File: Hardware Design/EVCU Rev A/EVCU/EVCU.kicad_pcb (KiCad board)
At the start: 4 copper layers, 121.9 x 86.4 mm, 91 parts, among them J1 Conn_01x06, J2 Conn_01x02, J3 APPS/BSE_Conn, J4 Micro_SD_Card, J5 DB9_Male, J6 Conn_01x02, Q1 Q_PMOS_GSD, U1 AZ1117-3.3, U10 EMIF06-MSD02N16, U11 ESDALC6V1W5, U2 AP62250WU-7, U3 STM32L4R9ZITx, U4 LM358, U5 MPU-6500, U6 SN65HVD230, U7 LM358, U9 ESDCAN24-2BLY, X1 ECS-2520MV-160-CN-TR

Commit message: bom. pcb. exports
- updated bom added q1, some other capacitors. updated component costs
- added logo to pcb
- changed swd pins to female socket
- exported gerbers
- filled out digikey order form
- filled out amazon order form
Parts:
- added G***: LOGO, LOGO, F.Cu at (108.0, 88.9)
- J1: footprint Connector_PinHeader_2.54mm:PinHeader_1x06_P2.54mm_Vertical -> Connector_PinSocket_2.54mm:PinSocket_1x06_P2.54mm_Vertical
- moved J3 0.86 mm to (18.8, 90.2)
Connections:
- net Net-(F1-Pad) renamed /F_OUT
- net Net-(J2-Pad1) renamed /F_IN
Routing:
- net /VPA_BSE: track 11.5 -> 12.4 mm
- net /VPA_2: track 10.7 -> 11.6 mm
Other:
- board text added: "VPA2"
- board text removed: "VPA 2"

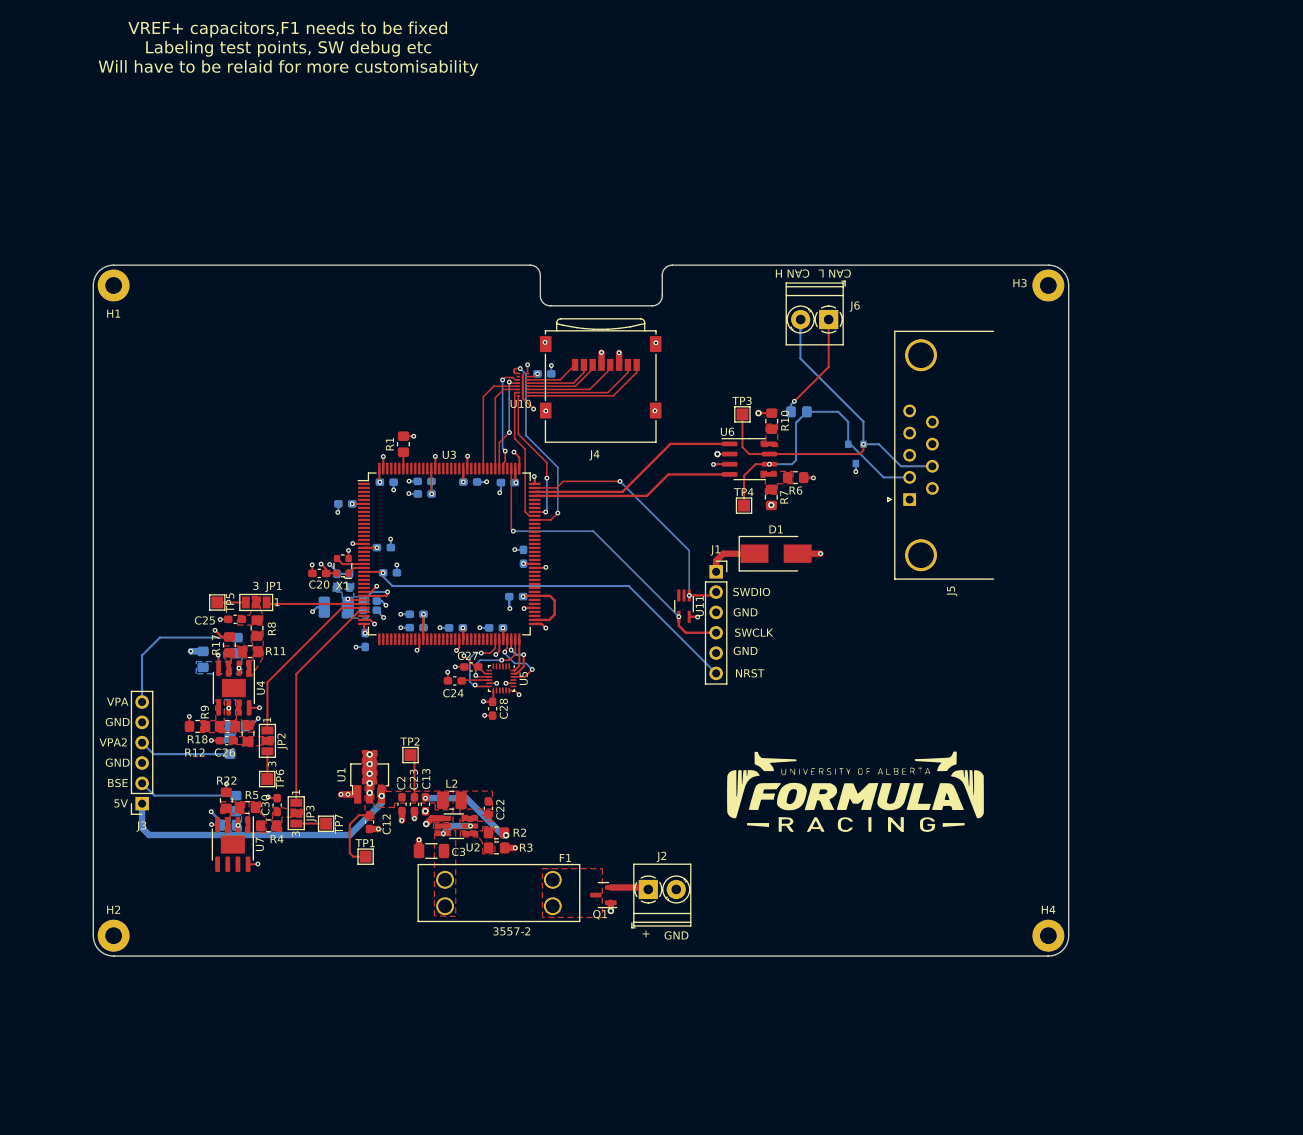
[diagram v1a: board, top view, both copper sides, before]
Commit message: pcb and bom
- moved mcu capacitors to top layer
- rearranged components to shrink pcb
- replaced j3 with 1x06 phoenix connector
- replaced j6 with 1x02 male 2.54 header
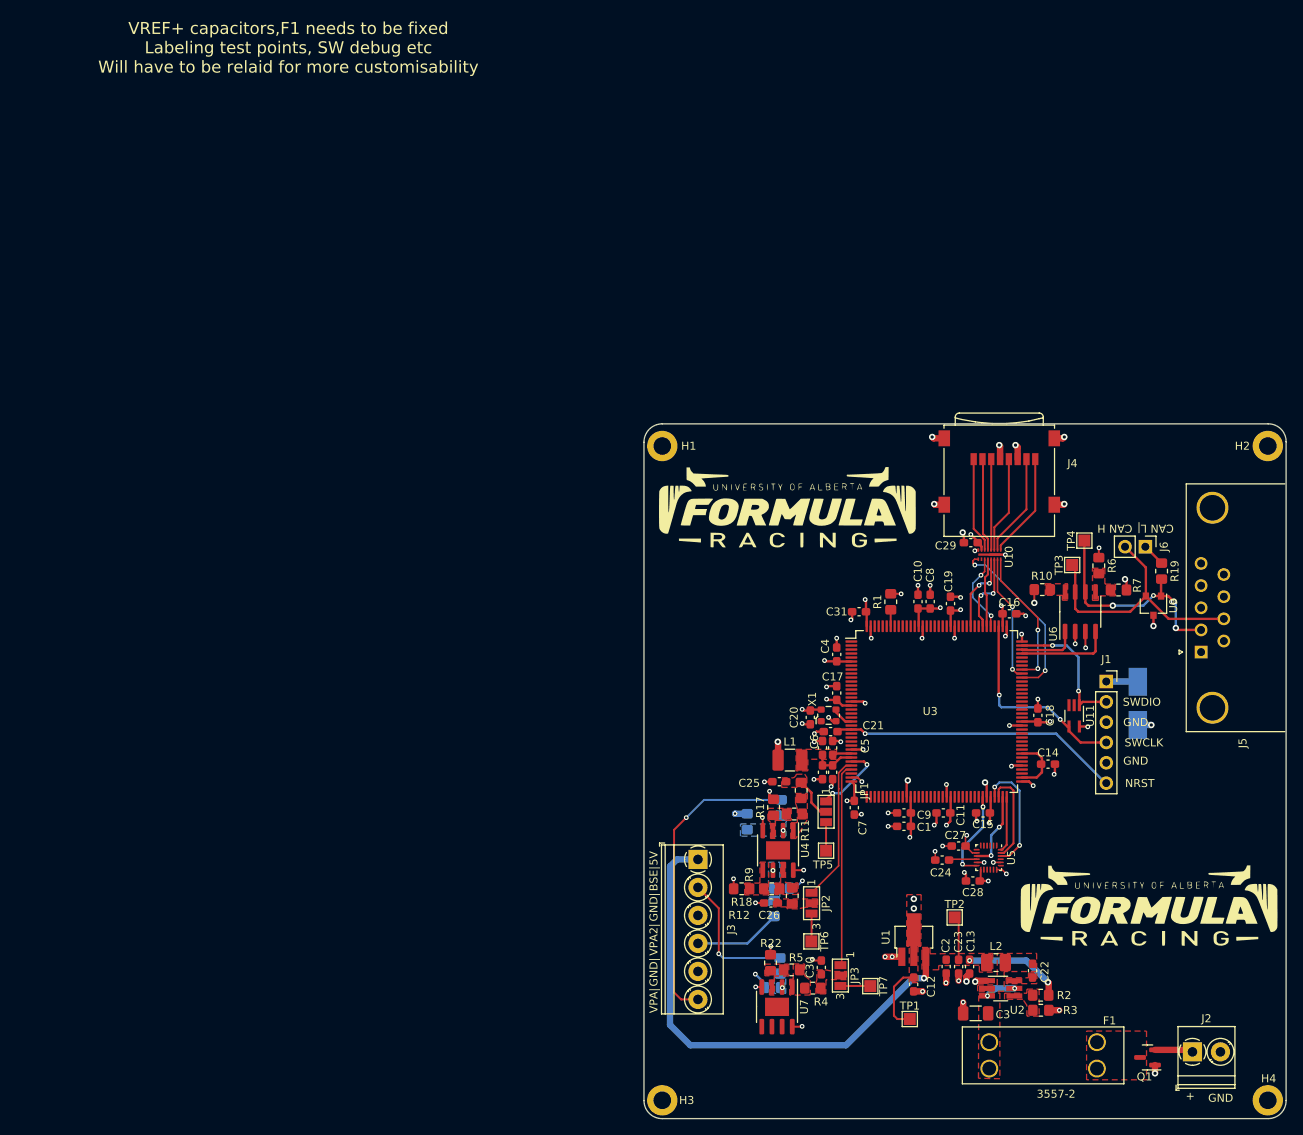
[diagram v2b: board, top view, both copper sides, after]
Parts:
- added G***: LOGO, LOGO, F.Cu at (144.7, 103.1)
- C1, C10, C11, C14, C15, C16, C17, C18, C19, C21, C29, C31, C32, C33, C4, C5, C6, C7, C8, C9, R19, U9: moved to F.Cu
- D1: moved to B.Cu
- H1, H2, H3, H4: footprint MountingHole:MountingHole_2.1mm -> MountingHole:MountingHole_2.2mm_M2_DIN965_Pad
- J3: footprint Connector_PinSocket_2.54mm:PinSocket_1x06_P2.54mm_Vertical -> TerminalBlock_Phoenix:TerminalBlock_Phoenix_PT-1,5-6-3.5-H_1x06_P3.50mm_Horizontal
- J6: footprint TerminalBlock_Phoenix:TerminalBlock_Phoenix_PT-1,5-2-3.5-H_1x02_P3.50mm_Horizontal -> Connector_PinHeader_2.54mm:PinHeader_1x02_P2.54mm_Vertical
- L1: value 39nH -> 100nH; moved to F.Cu
- moved H2 156.7 mm to (159.5, 45.5)
- moved H3 112.7 mm to (83.8, 127.3)
- moved TP5 82.2 mm to (104.3, 96.1), turned to 0 degrees
- moved JP1 75.9 mm to (104.3, 91.2), turned to -90 degrees
- moved H1 71.5 mm to (83.8, 45.5)
- moved C25 71.0 mm to (98.4, 87.4)
- moved JP2 71.0 mm to (102.5, 102.6)
- moved Q1 71.0 mm to (144.5, 121.9)
- moved R13 71.0 mm to (94.4, 92.4)
- moved R14 71.0 mm to (98.7, 100.7)
- moved R18 71.0 mm to (93.7, 100.8)
- moved R4 71.0 mm to (102.6, 113.2)
- moved R8 71.0 mm to (101.2, 88.5)
- moved U2 71.0 mm to (126.1, 113.3)
- moved U4 71.0 mm to (98.3, 96.0)
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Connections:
- net Net-(J6-Pad1) renamed /CAN_L_res
- J5 pad 0: (no net) -> GND
- U3 pad 22: /OSC_OUT -> unconnected-(U3-Pad22)
- X1 pad 1: /OSC_OUT -> unconnected-(X1-Pad1)
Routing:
- net +5V: track 53.4 -> 80.8 mm
- net /VPA: track 18.6 -> 38.6 mm, vias 0 -> 1
- net /CAN_TX: track 26.9 -> 7.53 mm
- net /CAN_H: track 49.1 -> 33.7 mm, vias 1 -> 0
- net /SWDIO: track 32.4 -> 17.3 mm
- net +3V3: track 62.3 -> 76.7 mm, vias 29 -> 26
- net /CAN_RX: track 25.5 -> 11.8 mm
- net /SWCLK: track 39.2 -> 25.5 mm
- net /NRST: track 49.6 -> 36.5 mm
- net /CAN_L_res: track 13.5 -> 2.89 mm, vias 1 -> 0
- net /CAN_L: track 35.5 -> 28.7 mm, vias 1 -> 4
- net /ACCEL_CS: track 8.92 -> 14.8 mm
- net /SCK: track 6.33 -> 11.7 mm, vias 2 -> 0
- net Net-(C25-Pad1): track 0.00 -> 5.36 mm
- net /FILTER_DAT2: track 6.72 -> 11.9 mm
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- added copper zone on F.Cu, net +3.3VA
- removed copper zone on B.Cu, net +3.3VA
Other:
- board size 121.9 x 86.4 mm -> 80.3 x 86.8 mm
- board text added: "BSE|"
- board text added: "CAN L|"
- board text added: "GND|"
- board text added: "VPA2|"
- board text added: "VPA|"
- board text removed: "BSE"
- board text removed: "CAN L"
- board text removed: "VPA"
- board text removed: "VPA2"

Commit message: more "final" changes
- simulated and redid op amp voltage scaling for 0-5V to 0-3.3V sensors
- decreased size of 3.3V copper pour
- grounded pcb and db9 mounting holes
- decreased size of board from 122x86 to 87x80 (in last commit but forgot to mention it)
- moved swd zener diode to top layer, no more components on bottom layer
- exported gerbers
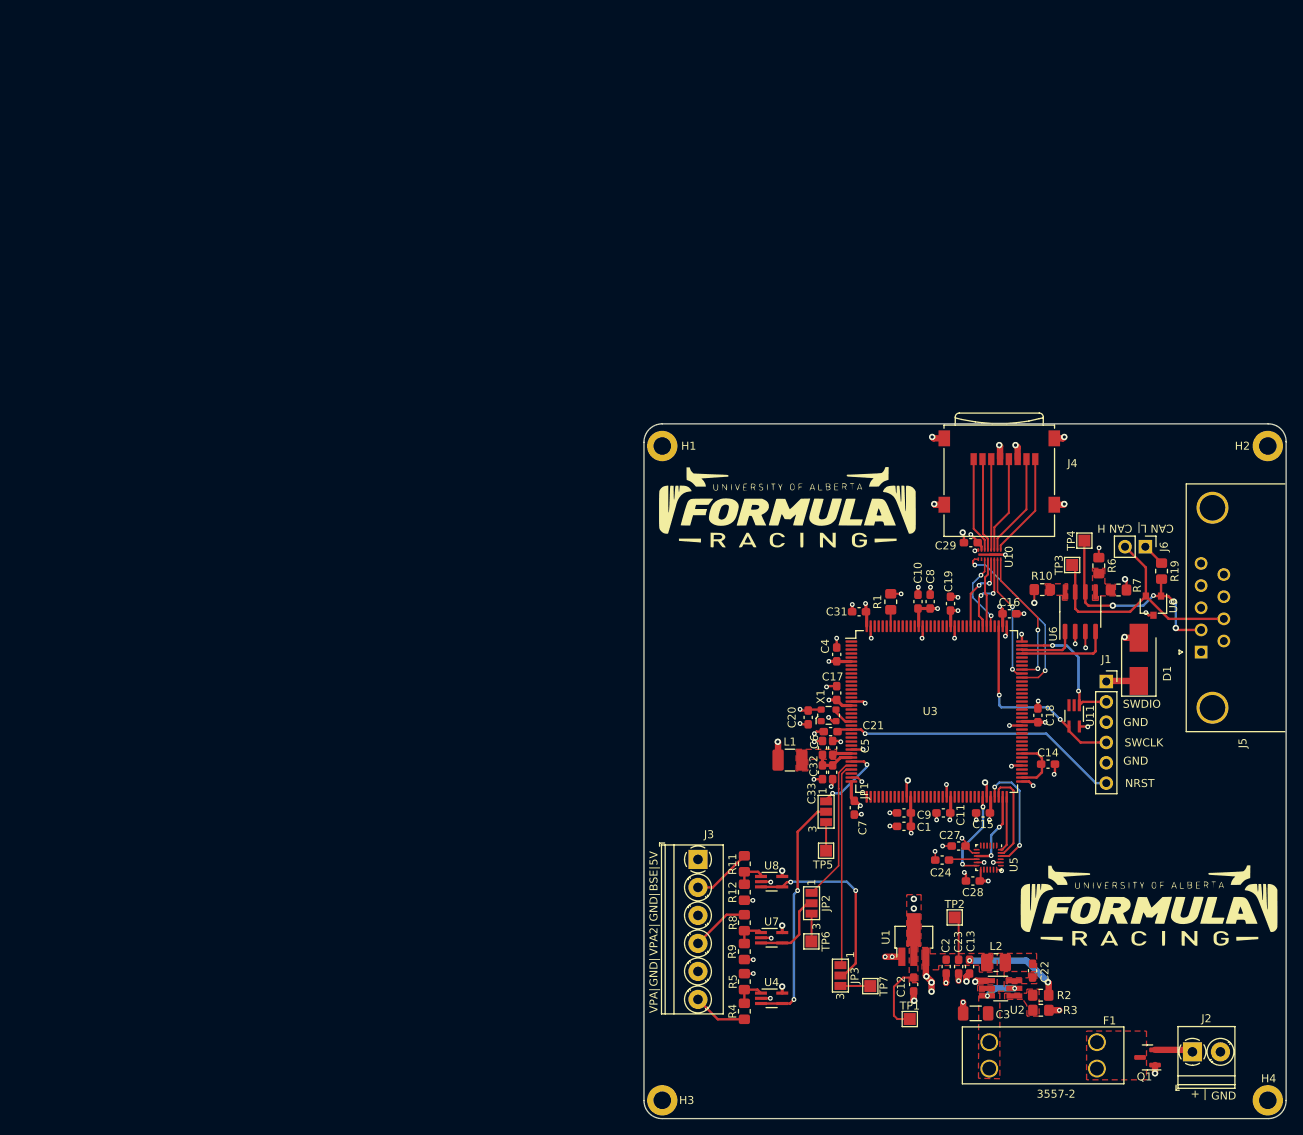
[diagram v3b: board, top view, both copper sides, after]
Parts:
- removed C25, C26, C30: 0.1uF, Capacitor_SMD:C_0603_1608Metric_Pad1.08x0.95mm_HandSolder
- removed R13, R14, R20: 34kR, Resistor_SMD:R_0805_2012Metric_Pad1.20x1.40mm_HandSolder
- removed R15, R16, R17, R18, R21, R22: 100kR, Resistor_SMD:R_0805_2012Metric_Pad1.20x1.40mm_HandSolder
- added U8: LMV321, Package_TO_SOT_SMD:SOT-353_SC-70-5_Handsoldering, F.Cu at (97.5, 99.9)
- D1: moved to F.Cu
- R11: value 33kR -> 50kR
- R12, R5: value 33kR -> 100kR
- R4, R8: value 100kR -> 50kR
- U4, U7: value LM358 -> LMV321; footprint Package_SO:SOIC-8-1EP_3.9x4.9mm_P1.27mm_EP2.29x3mm -> Package_TO_SOT_SMD:SOT-353_SC-70-5_Handsoldering
- moved U4 18.5 mm to (97.5, 114.5), turned to 0 degrees
- moved R8 18.0 mm to (94.1, 105.1)
- moved R9 9.18 mm to (94.1, 108.7), turned to -90 degrees
- moved R4 9.03 mm to (94.1, 116.1), turned to 90 degrees
- moved R11 8.81 mm to (94.1, 97.7), turned to -90 degrees
- moved U7 8.66 mm to (97.5, 106.9), turned to 0 degrees
- moved R5 6.09 mm to (94.1, 112.4), turned to 90 degrees
- moved D1 5.50 mm to (143.4, 72.1), turned to 90 degrees
- moved R12 3.45 mm to (94.1, 101.2), turned to -90 degrees
- moved C20 0.26 mm to (102.1, 79.4)
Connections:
- JP1 pad 2: Net-(C25-Pad1) -> /LMVAOUT
- JP2 pad 2: Net-(C26-Pad1) -> /LMVBOUT
- JP3 pad 2: Net-(C30-Pad1) -> /LMVCOUT
- R11 pad 1: /LMAOUT -> /VPA_BSE
- R11 pad 2: /LMA+ -> /LMA+_BSE
- R12 pad 1: /LMBOUT -> /LMA+_BSE
- R12 pad 2: /LMB+ -> GND
- R4 pad 1: Net-(C30-Pad1) -> /VPA
- R4 pad 2: /LMAOUT_BSE -> /LMA+
- R5 pad 1: /LMAOUT_BSE -> /LMA+
- R5 pad 2: /LMA+_BSE -> GND
- R8 pad 1: Net-(C25-Pad1) -> /VPA_2
- R8 pad 2: /LMAOUT -> /LMB+
- R9 pad 1: Net-(C26-Pad1) -> /LMB+
- R9 pad 2: /LMBOUT -> GND
- U4 pad 1: /LMAOUT -> /LMA+
- U4 pad 2: /LMA- -> GND
- U4 pad 3: /LMA+ -> /LMVAOUT
- U4 pad 4: GND -> /LMVAOUT
- U4 pad 5: /LMB+ -> +5V
- U7 pad 1: /LMAOUT_BSE -> /LMB+
- U7 pad 2: /LMA-_BSE -> GND
- U7 pad 3: /LMA+_BSE -> /LMVBOUT
- U7 pad 4: GND -> /LMVBOUT
- U7 pad 5: unconnected-(U7-Pad5) -> +5V
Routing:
- net +5V: track 80.8 -> 25.2 mm, vias 3 -> 8
- net /VPA: track 38.6 -> 6.83 mm, vias 1 -> 0
- net /LMVAOUT: track 0.00 -> 30.1 mm, vias 0 -> 2
- net /LMVCOUT: track 0.00 -> 24.2 mm, vias 0 -> 2
- net GND: track 97.5 -> 86.1 mm, vias 74 -> 69
- net /LMVBOUT: track 0.00 -> 10.1 mm
- net /VPA_BSE: track 17.3 -> 7.44 mm, vias 1 -> 0
- net +3V3: track 76.7 -> 69.8 mm, vias 26 -> 24
- net Net-(C25-Pad1): track 5.36 -> 0.00 mm
- net /LMA+_BSE: track 0.00 -> 4.00 mm
- net /LMA+: track 0.00 -> 3.96 mm
- net /LMB+: track 0.00 -> 3.78 mm
- net /VPA_2: track 10.9 -> 7.29 mm
- net /LMB-: vias 1 -> 0
- net /LMA-_BSE: vias 1 -> 0
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- added copper zone on In2.Cu, net +5V
- removed copper zone on F.Cu, net /LMA+
- removed copper zone on F.Cu, net /LMA+_BSE
- removed copper zone on B.Cu, net /LMA-
- removed copper zone on B.Cu, net /LMA-_BSE
- removed copper zone on F.Cu, net /LMAOUT
- removed copper zone on F.Cu, net /LMAOUT_BSE
- removed copper zone on F.Cu, net /LMB+
- removed copper zone on B.Cu, net /LMB-
- removed copper zone on F.Cu, net /LMBOUT
- removed copper zone on F.Cu, net Net-(C25-Pad1)
- removed copper zone on F.Cu, net Net-(C26-Pad1)
- removed copper zone on F.Cu, net Net-(C30-Pad1)
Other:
- board text added: "+ |"
- board text removed: "+"
- board text removed: "VREF+ capacitors,F1 needs to be fixed Labeling test points, SW debug etc Will have to be relaid for more customisability"

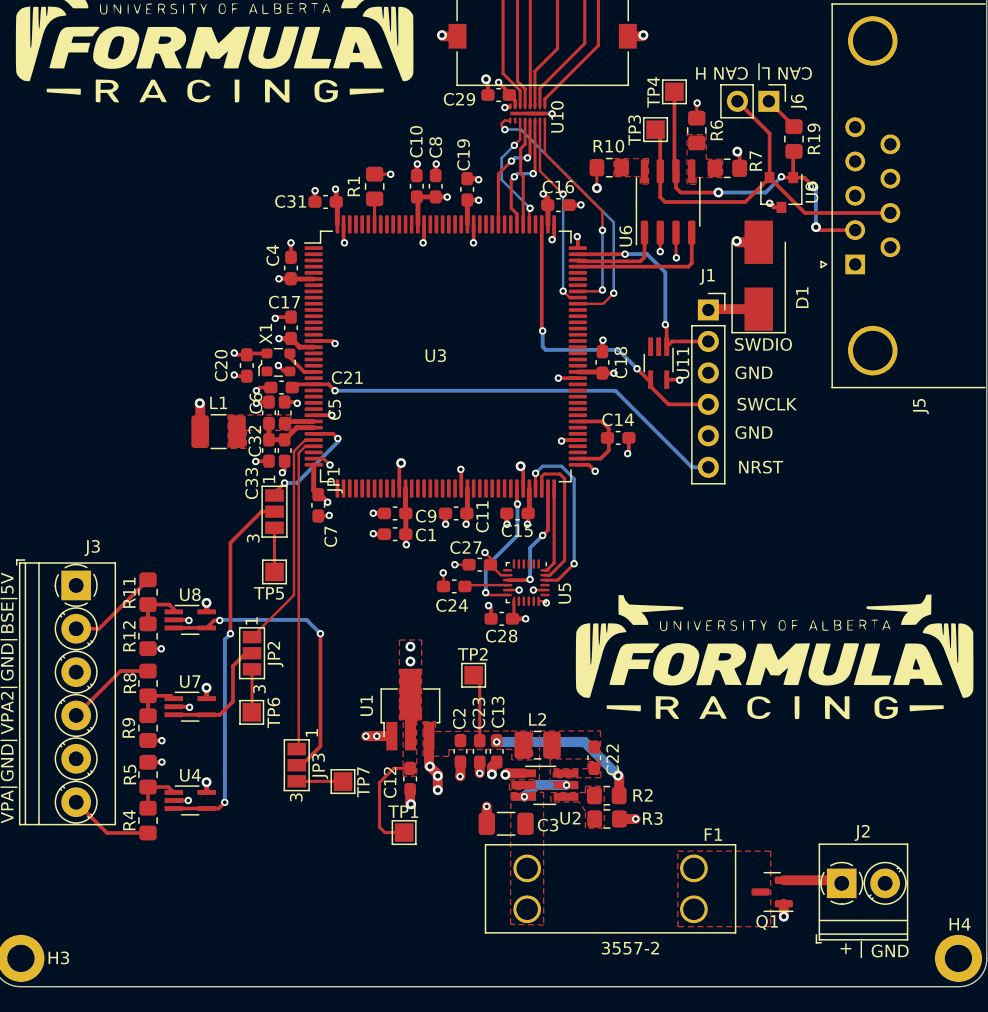
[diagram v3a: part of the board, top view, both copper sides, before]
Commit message: cleaning up courtyard spacing
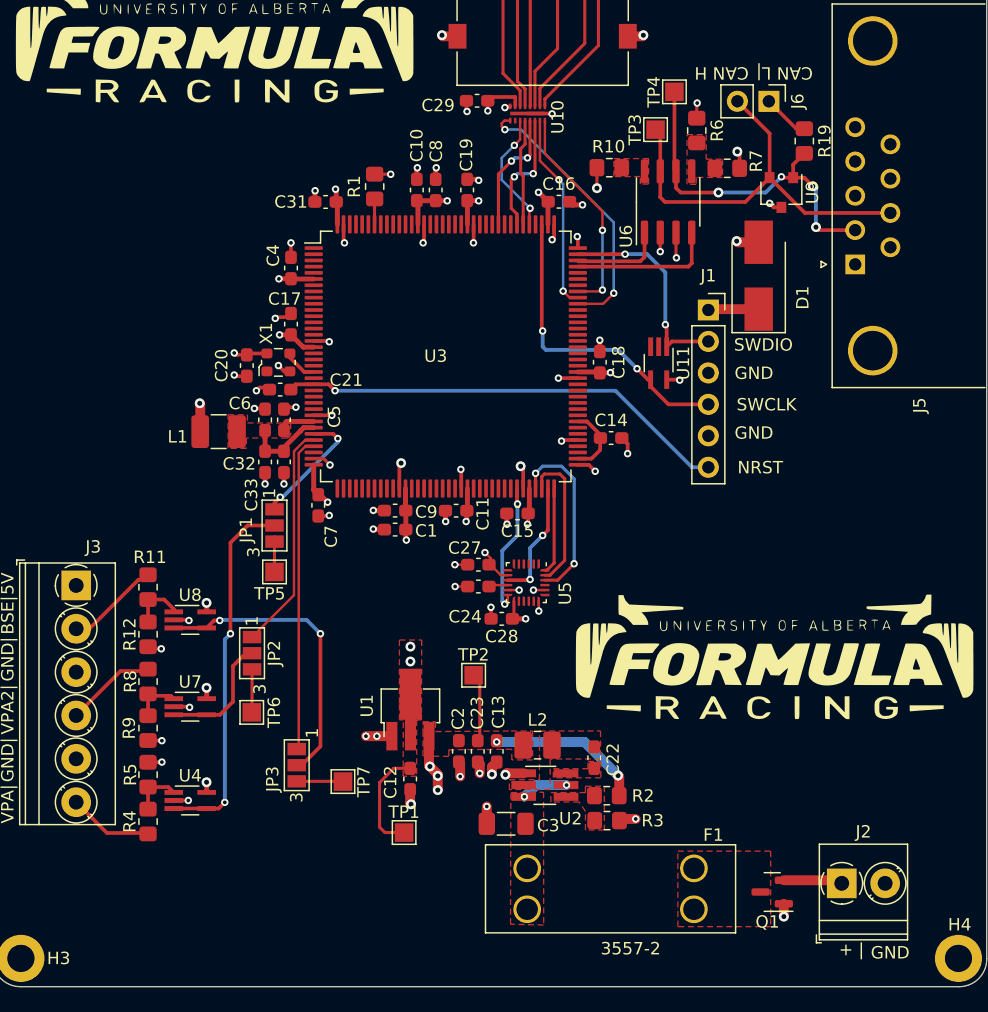
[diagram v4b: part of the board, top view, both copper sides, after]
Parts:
- moved C24 1.95 mm to (120.8, 97.2)
- moved C29 1.80 mm to (120.7, 58.0)
- moved JP1 1.12 mm to (104.3, 92.3)
- moved C32 0.98 mm to (103.5, 87.2)
- moved C33 0.93 mm to (105.1, 87.2)
- moved R19 0.85 mm to (147.1, 61.3)
- moved C6 0.65 mm to (103.5, 83.8)
- moved C5 0.57 mm to (105.1, 83.8)
- moved C14 0.57 mm to (131.5, 85.2)
- moved R11 0.41 mm to (94.1, 97.3)
- moved C1 0.37 mm to (114.0, 92.6)
- moved C10 0.30 mm to (115.8, 65.2)
- moved C8 0.30 mm to (117.3, 65.2)
- moved C17 0.30 mm to (105.6, 76.0)
- moved C16 0.27 mm to (127.3, 66.2)
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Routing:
- net Net-(C24-Pad1): track 3.50 -> 1.55 mm
- net /VSI: track 7.27 -> 5.57 mm
- net +3.3VA: track 7.75 -> 8.98 mm
- net GND: track 86.1 -> 84.9 mm
- net +3V3: track 69.8 -> 71.0 mm
- net /CAN_L_res: track 2.89 -> 3.78 mm
- net /VOUT_1_APPS: track 9.41 -> 10.1 mm
- net Net-(JP1-Pad3): track 2.84 -> 2.24 mm
- net /LMA+_BSE: track 4.00 -> 4.58 mm
- net /INT: track 11.3 -> 10.8 mm
